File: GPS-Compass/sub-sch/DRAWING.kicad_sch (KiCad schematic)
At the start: 0 parts

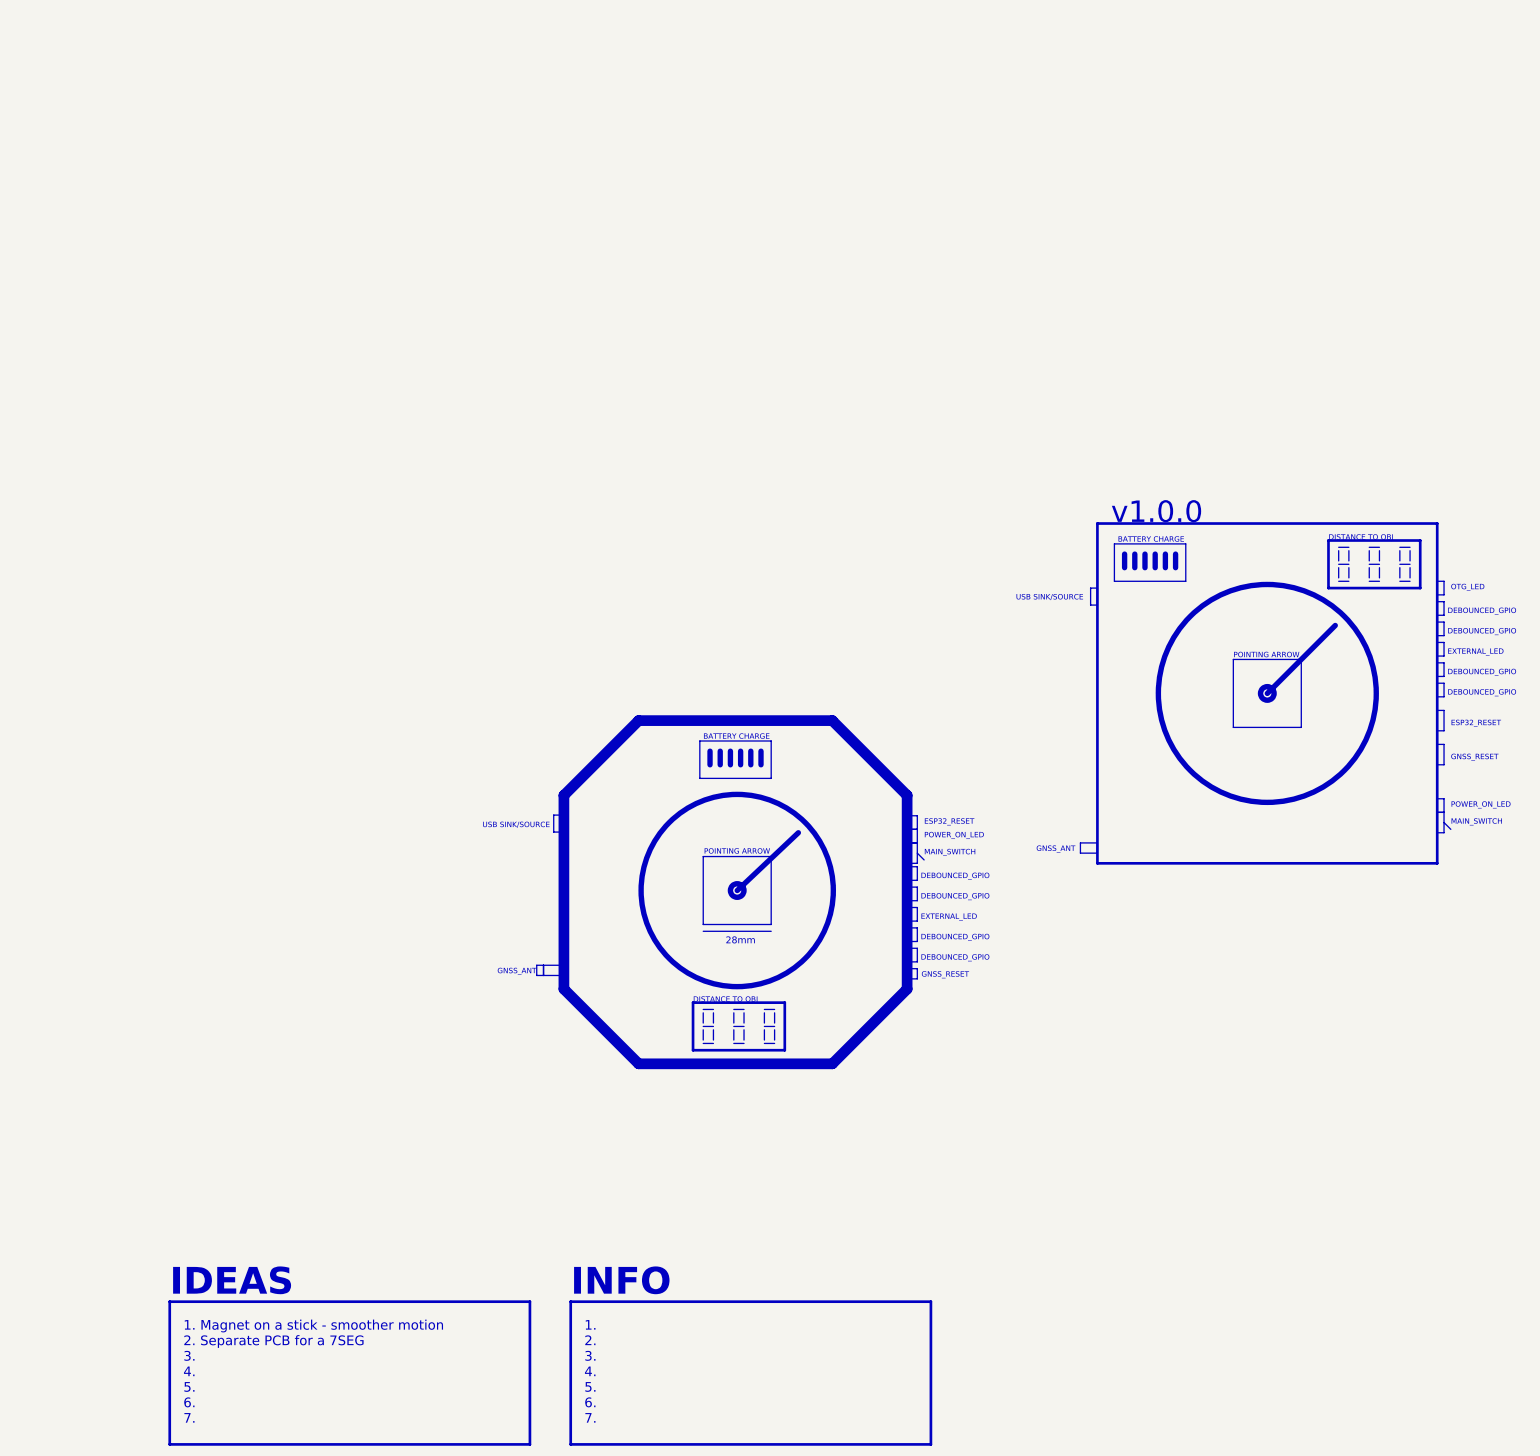
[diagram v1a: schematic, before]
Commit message: schematic update
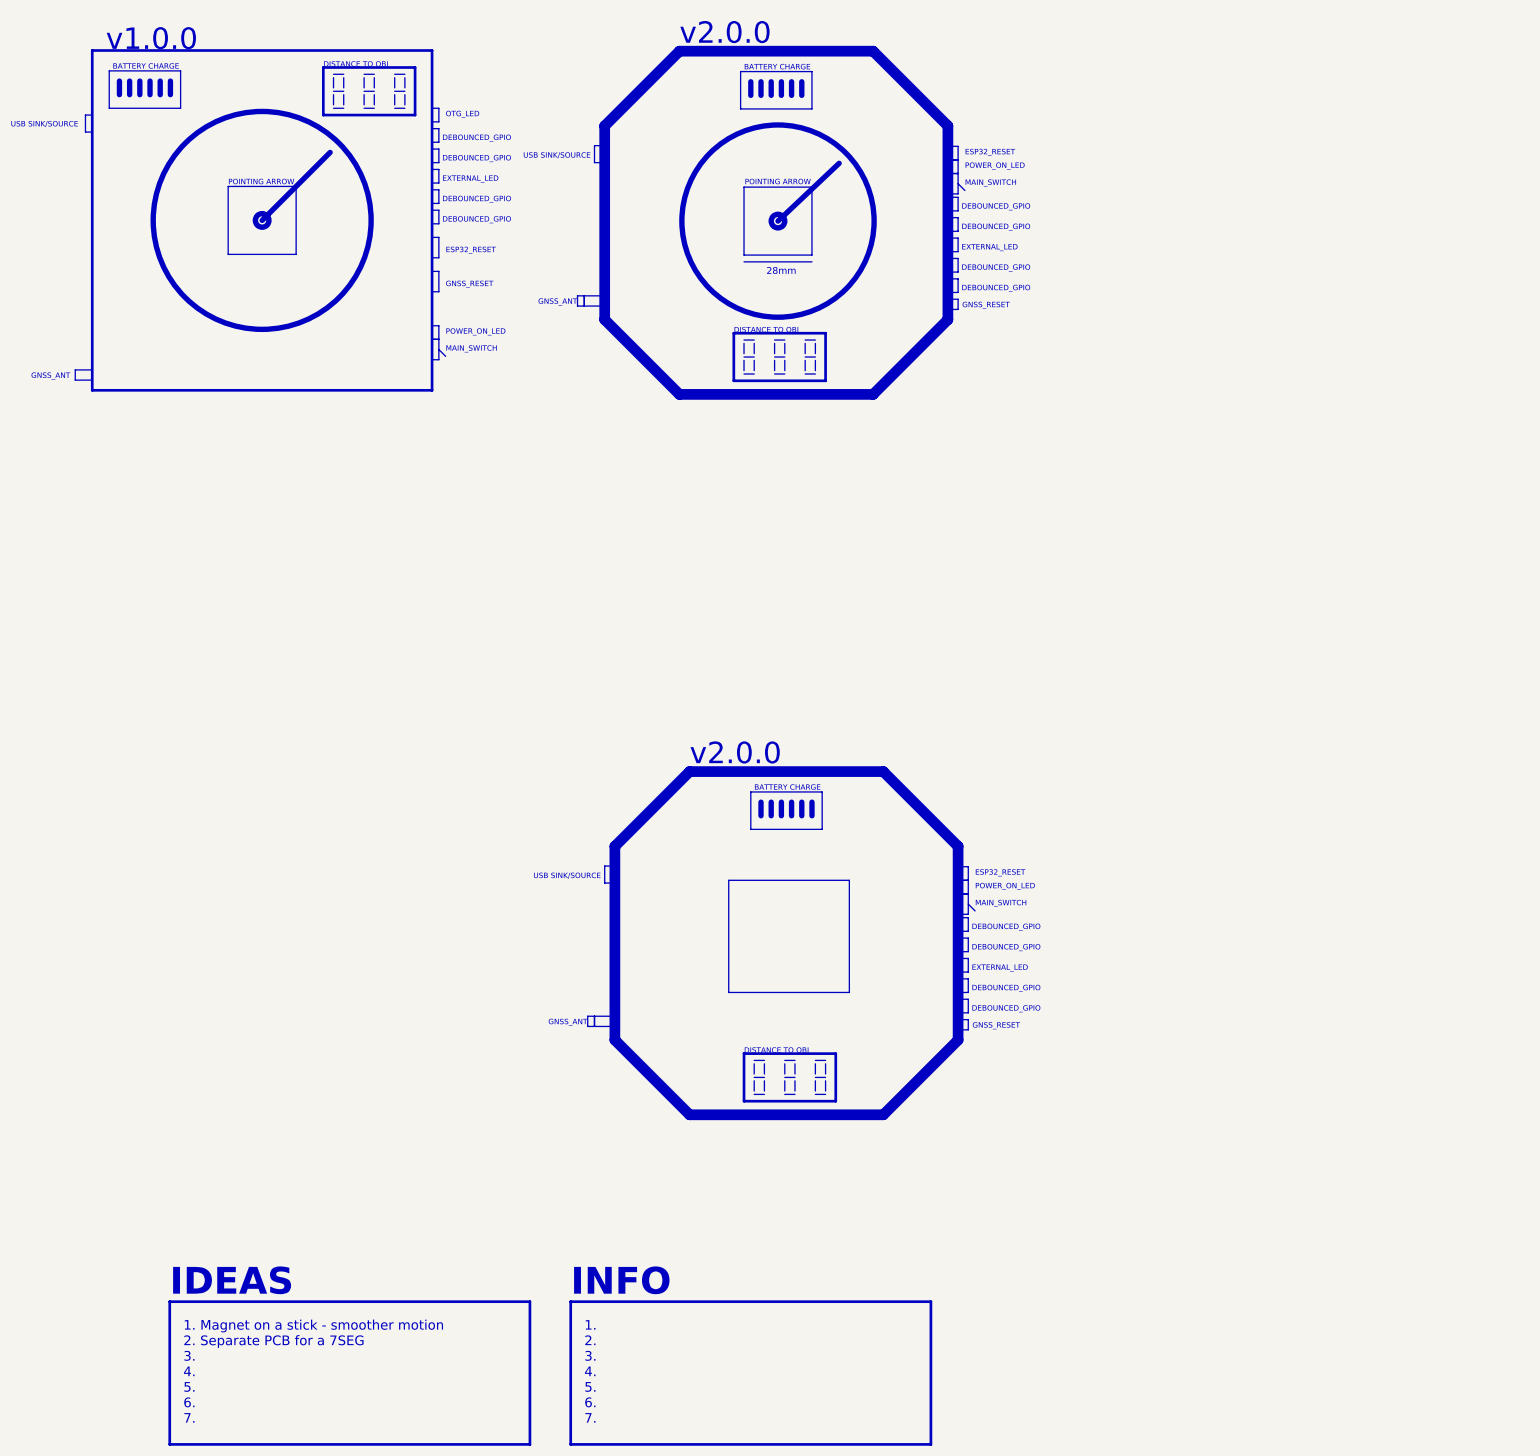
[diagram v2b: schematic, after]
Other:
- note added: "v2.0.0"
